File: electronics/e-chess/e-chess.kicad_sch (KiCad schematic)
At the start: 7 parts, among them SW1 SW_Reed, U1 MCP23017_SP, U2 ESP32-S3

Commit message: Fix led order docu
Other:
- note added: "In total 64 LEDs: Running in horízontal snake lines from the top right to the bottom right."
- note removed: "In total 64 LEDs: Running in horízontal snake lines from the top right to the bottom left."
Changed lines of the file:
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@@
 		)
 	)
-	(text "In total 64 LEDs:\nRunning in horízontal snake lines \nfrom the top right to the bottom left."
+	(text "In total 64 LEDs:\nRunning in horízontal snake lines \nfrom the top right to the bottom right."
 		(exclude_from_sim no)
 		(at 37.846 66.548 0)

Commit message: Add link to https://www.instructables.com/Low-Cost-Automation-ESP32-and-16-Relays/
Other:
- note added: "See https://www.instructables.com/Low-Cost-Automation-ESP32-and-16-Relays/"
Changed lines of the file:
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@@
+		)
+	)
+	(text "See https://www.instructables.com/Low-Cost-Automation-ESP32-and-16-Relays/"
+		(exclude_from_sim no)
+		(at 240.538 30.48 0)
+		(effects
+			(font
+				(size 1.27 1.27)
+			)
 		)
 	)

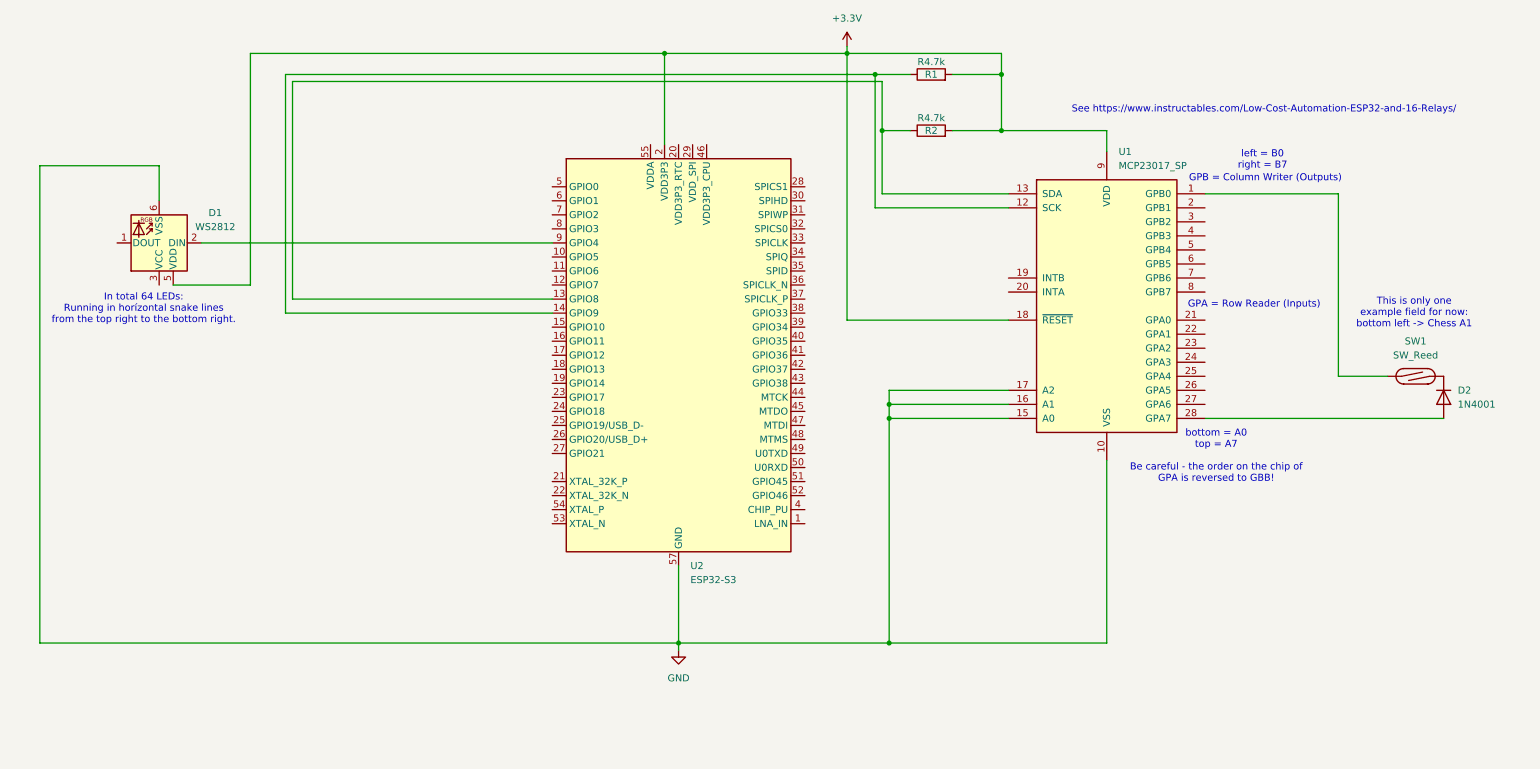
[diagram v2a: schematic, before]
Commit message: Improve electroinic schmeatics
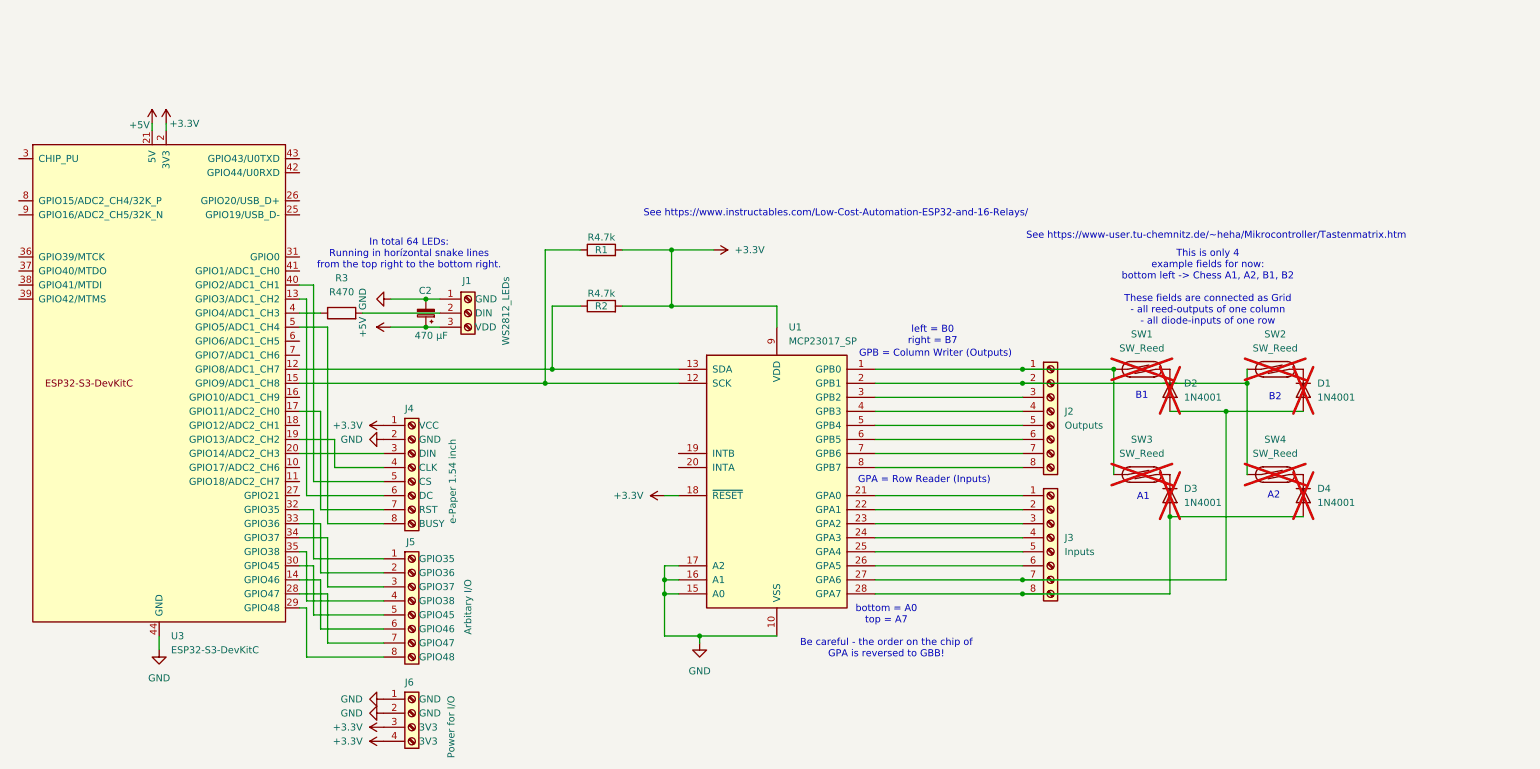
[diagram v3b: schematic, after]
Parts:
- removed D1: WS2812, LED_SMD:LED_WS2812_PLCC6_5.0x5.0mm_P1.6mm, symbol LED:WS2812
- removed U2: ESP32-S3, Package_DFN_QFN:QFN-56-1EP_7x7mm_P0.4mm_EP4x4mm, symbol MCU_Espressif:ESP32-S3
- added C2: 470 µF, symbol Device:C_Polarized_Small
- added D1, D3, D4: 1N4001, Diode_THT:D_DO-41_SOD81_P10.16mm_Horizontal, symbol Diode:1N4001
- added J1: WS2812_LEDs, TerminalBlock_Phoenix:TerminalBlock_Phoenix_MKDS-1,5-3-5.08_1x03_P5.08mm_Horizontal, symbol Connector:Screw_Terminal_01x03
- added J2: Outputs, symbol Connector:Screw_Terminal_01x08
- added J3: Inputs, symbol Connector:Screw_Terminal_01x08
- added J4: e-Paper 1.54 inch, TerminalBlock_Phoenix:TerminalBlock_Phoenix_MKDS-1,5-8-5.08_1x08_P5.08mm_Horizontal, symbol Connector:Screw_Terminal_01x08
- added J5: Arbitary I/O, TerminalBlock_Phoenix:TerminalBlock_Phoenix_MKDS-1,5-8-5.08_1x08_P5.08mm_Horizontal, symbol Connector:Screw_Terminal_01x08
- added J6: Power for I/O, symbol Connector:Screw_Terminal_01x04
- added R3: R470, symbol Device:R
- added SW2, SW3, SW4: SW_Reed, symbol Switch:SW_Reed
- added U3: ESP32-S3-DevKitC, PCM_Espressif:ESP32-S3-DevKitC, symbol PCM_Espressif:ESP32-S3-DevKitC
- D2, SW1: now not fitted; now left out of the parts list
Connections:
- net +3.3V: now also J4.1 (VCC), J6.3 (3V3), J6.4 (3V3), U3.1 (3V3), U3.2 (3V3)
- net GND: now also C2.2, J1.1 (GND), J4.2 (GND), J6.1 (GND), J6.2 (GND), U3.22 (GND), U3.23 (GND), U3.24 (GND), U3.44 (GND)
- net at SW1.1, U1.1 (GPB0): now also J2.1 (Pin_1), SW3.1
- net at R1.1, U1.12 (SCK): now also U3.15 (GPIO9/ADC1_CH8)
- net at R2.1, U1.13 (SDA): now also U3.12 (GPIO8/ADC1_CH7)
- net at U1.2 (GPB1): now also J2.2 (Pin_2), SW2.1, SW4.1
- net at U1.21 (GPA0): now also J3.1 (Pin_1)
- net at U1.22 (GPA1): now also J3.2 (Pin_2)
- net at U1.23 (GPA2): now also J3.3 (Pin_3)
- net at U1.24 (GPA3): now also J3.4 (Pin_4)
- net at U1.25 (GPA4): now also J3.5 (Pin_5)
- net at U1.26 (GPA5): now also J3.6 (Pin_6)
- net at U1.27 (GPA6): now also D2.2 (A), D1.2 (A), J3.7 (Pin_7)
- net at U1.28 (GPA7): now also D3.2 (A), D4.2 (A), J3.8 (Pin_8); no longer D2.2 (A)
- net at U1.3 (GPB2): now also J2.3 (Pin_3)
- net at U1.4 (GPB3): now also J2.4 (Pin_4)
- net at U1.5 (GPB4): now also J2.5 (Pin_5)
- net at U1.6 (GPB5): now also J2.6 (Pin_6)
- net at U1.7 (GPB6): now also J2.7 (Pin_7)
- net at U1.8 (GPB7): now also J2.8 (Pin_8)
- new net: J4.6 (DC), U3.13 (GPIO3/ADC1_CH2)
- new net: J5.6 (GPIO46), U3.14 (GPIO46)
- new net: J4.7 (RST), U3.17 (GPIO11/ADC2_CH0)
- new net: J4.4 (CLK), U3.19 (GPIO13/ADC2_CH2)
- new net: J4.3 (DIN), U3.20 (GPIO14/ADC2_CH3)
- new net: J5.7 (GPIO47), U3.28 (GPIO47)
- new net: J5.8 (GPIO48), U3.29 (GPIO48)
- new net: J5.5 (GPIO45), U3.30 (GPIO45)
- new net: J5.1 (GPIO35), U3.32 (GPIO35)
- new net: J5.2 (GPIO36), U3.33 (GPIO36)
- new net: J5.3 (GPIO37), U3.34 (GPIO37)
- new net: J5.4 (GPIO38), U3.35 (GPIO38)
- new net: R3.1, U3.4 (GPIO4/ADC1_CH3)
- new net: J4.5 (CS), U3.40 (GPIO2/ADC1_CH1)
- new net: J4.8 (BUSY), U3.5 (GPIO5/ADC1_CH4)
- new net: D1.1 (K), SW2.2
- new net: J1.2 (DIN), R3.2
- new net: D4.1 (K), SW4.2
- new net: D3.1 (K), SW3.2
- new net +5V: C2.1, J1.3 (VDD), U3.21 (5V)
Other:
- note added: "A1"
- note added: "A2"
- note added: "B1"
- note added: "B2"
- note added: "See https://www-user.tu-chemnitz.de/~heha/Mikrocontroller/Tastenmatrix.htm"
- note added: "This is only 4 example fields for now: bottom left -> Chess A1, A2, B1, B2 These fields are connected as Grid - all reed-outputs of one column - all diode-inputs of one row"
- note removed: "This is only one example field for now: bottom left -> Chess A1"
- moved on the sheet: R1, R2, U1

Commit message: Draw PCB
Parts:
- C2: footprint (none) -> Capacitor_THT:CP_Radial_D10.0mm_P5.00mm
- J2, J3: footprint (none) -> TerminalBlock_Phoenix:TerminalBlock_Phoenix_MKDS-1,5-8-5.08_1x08_P5.08mm_Horizontal
- J6: footprint (none) -> TerminalBlock_Phoenix:TerminalBlock_Phoenix_MKDS-1,5-4-5.08_1x04_P5.08mm_Horizontal
- R1, R2, R3: footprint (none) -> Resistor_THT:R_Axial_DIN0207_L6.3mm_D2.5mm_P7.62mm_Horizontal
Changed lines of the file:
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@@
 			)
 		)
-		(property "Footprint" ""
+		(property "Footprint" "TerminalBlock_Phoenix:TerminalBlock_Phoenix_MKDS-1,5-8-5.08_1x08_P5.08mm_Horizontal"
 			(at 201.93 85.09 0)
 			(effects
@@
 			)
 		)
-		(property "Footprint" ""
+		(property "Footprint" "Resistor_THT:R_Axial_DIN0207_L6.3mm_D2.5mm_P7.62mm_Horizontal"
 			(at 73.66 69.088 90)
 			(effects
@@
 			)
 		)
-		(property "Footprint" ""
+		(property "Footprint" "Capacitor_THT:CP_Radial_D10.0mm_P5.00mm"
 			(at 88.9 67.31 0)
 			(effects
@@
 			)
 		)
-		(property "Footprint" ""
+		(property "Footprint" "TerminalBlock_Phoenix:TerminalBlock_Phoenix_MKDS-1,5-4-5.08_1x04_P5.08mm_Horizontal"
 			(at 86.36 139.7 0)
 			(effects
@@
 			)
 		)
-		(property "Footprint" ""
+		(property "Footprint" "TerminalBlock_Phoenix:TerminalBlock_Phoenix_MKDS-1,5-8-5.08_1x08_P5.08mm_Horizontal"
 			(at 201.93 107.95 0)
 			(effects
@@
 			)
 		)
-		(property "Footprint" ""
+		(property "Footprint" "Resistor_THT:R_Axial_DIN0207_L6.3mm_D2.5mm_P7.62mm_Horizontal"
 			(at 120.65 57.658 90)
 			(effects
@@
 			)
 		)
-		(property "Footprint" ""
+		(property "Footprint" "Resistor_THT:R_Axial_DIN0207_L6.3mm_D2.5mm_P7.62mm_Horizontal"
 			(at 120.65 67.818 90)
 			(effects

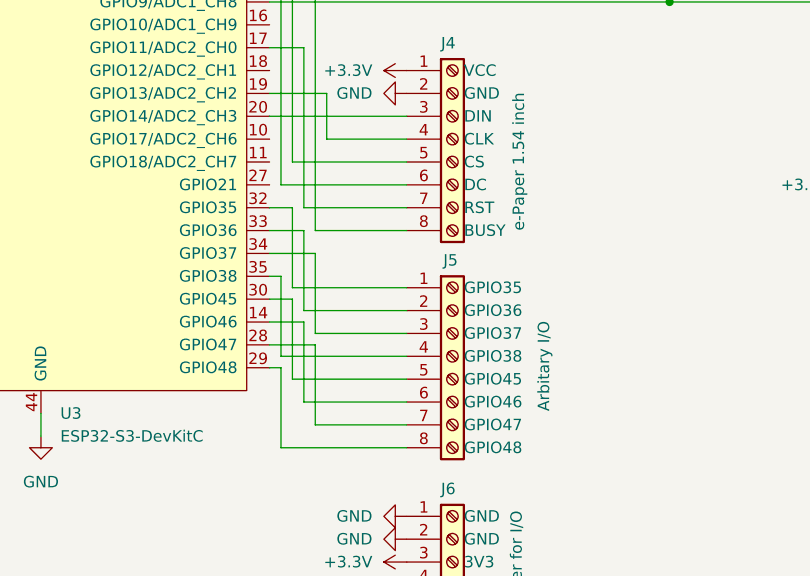
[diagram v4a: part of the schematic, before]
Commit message: change exposed pins a bit
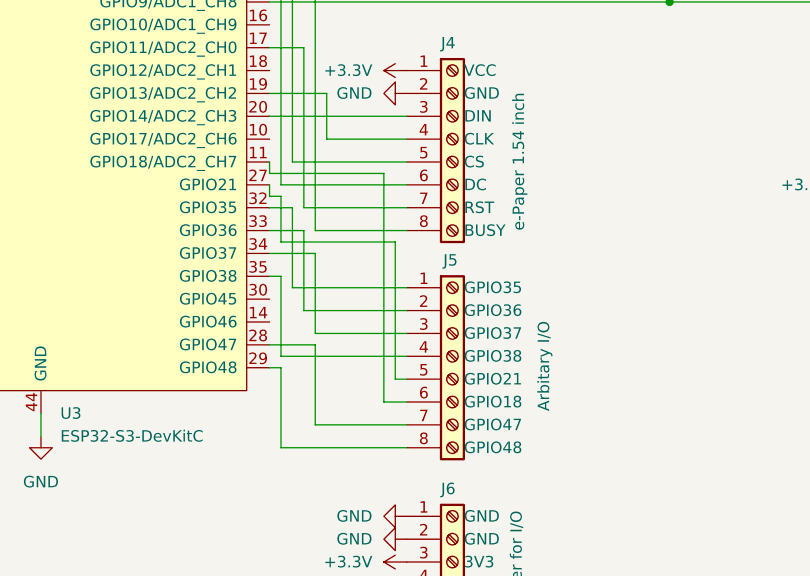
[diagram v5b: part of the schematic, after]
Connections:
- net at U3.11 (GPIO18/ADC2_CH7): now also J5.6 (GPIO18)
- net at U3.14 (GPIO46): no longer J5.6 (GPIO46)
- net at U3.27 (GPIO21): now also J5.5 (GPIO21)
- net at U3.30 (GPIO45): no longer J5.5 (GPIO45)
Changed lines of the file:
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@@
+	(wire
+		(pts
+			(xy 67.31 101.6) (xy 67.31 106.68)
+		)
+		(stroke
+			(width 0)
+			(type default)
+		)
+	)
 	(wire
 		(pts
@@
 	(wire
 		(pts
+			(xy 67.31 106.68) (xy 80.01 106.68)
+		)
+		(stroke
+			(width 0)
+			(type default)
+		)
+	)
+	(wire
+		(pts
+			(xy 80.01 121.92) (xy 81.28 121.92)
+		)
+		(stroke
+			(width 0)
+			(type default)
+		)
+	)
+	(wire
+		(pts
 			(xy 71.12 127) (xy 81.28 127)
 		)
@@
 	(wire
 		(pts
+			(xy 66.04 97.79) (xy 66.04 99.06)
+		)
+		(stroke
+			(width 0)
+			(type default)
+		)
+	)
+	(wire
+		(pts
 			(xy 67.31 119.38) (xy 81.28 119.38)
 		)
@@
 	(wire
 		(pts
-			(xy 68.58 113.03) (xy 68.58 121.92)
-		)
-		(stroke
-			(width 0)
-			(type default)
-		)
-	)
-	(wire
-		(pts
 			(xy 170.18 110.49) (xy 196.85 110.49)
 		)
@@
 	(wire
 		(pts
-			(xy 69.85 124.46) (xy 81.28 124.46)
-		)
-		(stroke
-			(width 0)
-			(type default)
-		)
-	)
-	(wire
-		(pts
 			(xy 66.04 85.09) (xy 69.85 85.09)
 		)
@@
 	(wire
 		(pts
+			(xy 78.74 124.46) (xy 81.28 124.46)
+		)
+		(stroke
+			(width 0)
+			(type default)
+		)
+	)
+	(wire
+		(pts
 			(xy 111.76 77.47) (xy 111.76 66.04)
 		)
@@
 	(wire
 		(pts
-			(xy 66.04 113.03) (xy 68.58 113.03)
-		)
-		(stroke
-			(width 0)
-			(type default)
-		)
-	)
-	(wire
-		(pts
 			(xy 66.04 77.47) (xy 111.76 77.47)
 		)
@@
 	(wire
 		(pts
+			(xy 66.04 99.06) (xy 78.74 99.06)
+		)
+		(stroke
+			(width 0)
+			(type default)
+		)
+	)
+	(wire
+		(pts
 			(xy 66.04 67.31) (xy 69.85 67.31)
 		)
@@
 	(wire
 		(pts
+			(xy 80.01 106.68) (xy 80.01 121.92)
+		)
+		(stroke
+			(width 0)
+			(type default)
+		)
+	)
+	(wire
+		(pts
 			(xy 69.85 114.3) (xy 81.28 114.3)
 		)
@@
 	(wire
 		(pts
+			(xy 78.74 99.06) (xy 78.74 124.46)
+		)
+		(stroke
+			(width 0)
+			(type default)
+		)
+	)
+	(wire
+		(pts
 			(xy 71.12 107.95) (xy 71.12 116.84)
 		)
@@
 	(wire
 		(pts
-			(xy 68.58 121.92) (xy 81.28 121.92)
+			(xy 66.04 101.6) (xy 67.31 101.6)
 		)
 		(stroke
@@
 	(wire
 		(pts
-			(xy 66.04 115.57) (xy 69.85 115.57)
-		)
-		(stroke
-			(width 0)
-			(type default)
-		)
-	)
-	(wire
-		(pts
 			(xy 69.85 105.41) (xy 69.85 114.3)
 		)
@@
 	(wire
 		(pts
-			(xy 69.85 115.57) (xy 69.85 124.46)
-		)
-		(stroke
-			(width 0)
-			(type default)
-		)
-	)
-	(wire
-		(pts
 			(xy 196.85 77.47) (xy 170.18 77.47)
 		)
@@
 		)
 		(stroke
+			(width 0)
+			(type default)
+		)
+	)
+	(wire
+		(pts
+			(xy 66.04 100.33) (xy 66.04 101.6)
+		)
+		(stroke
